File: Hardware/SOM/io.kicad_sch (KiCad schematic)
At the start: 1 part, among them U1 LFE5UM5G-85F-8BG381x

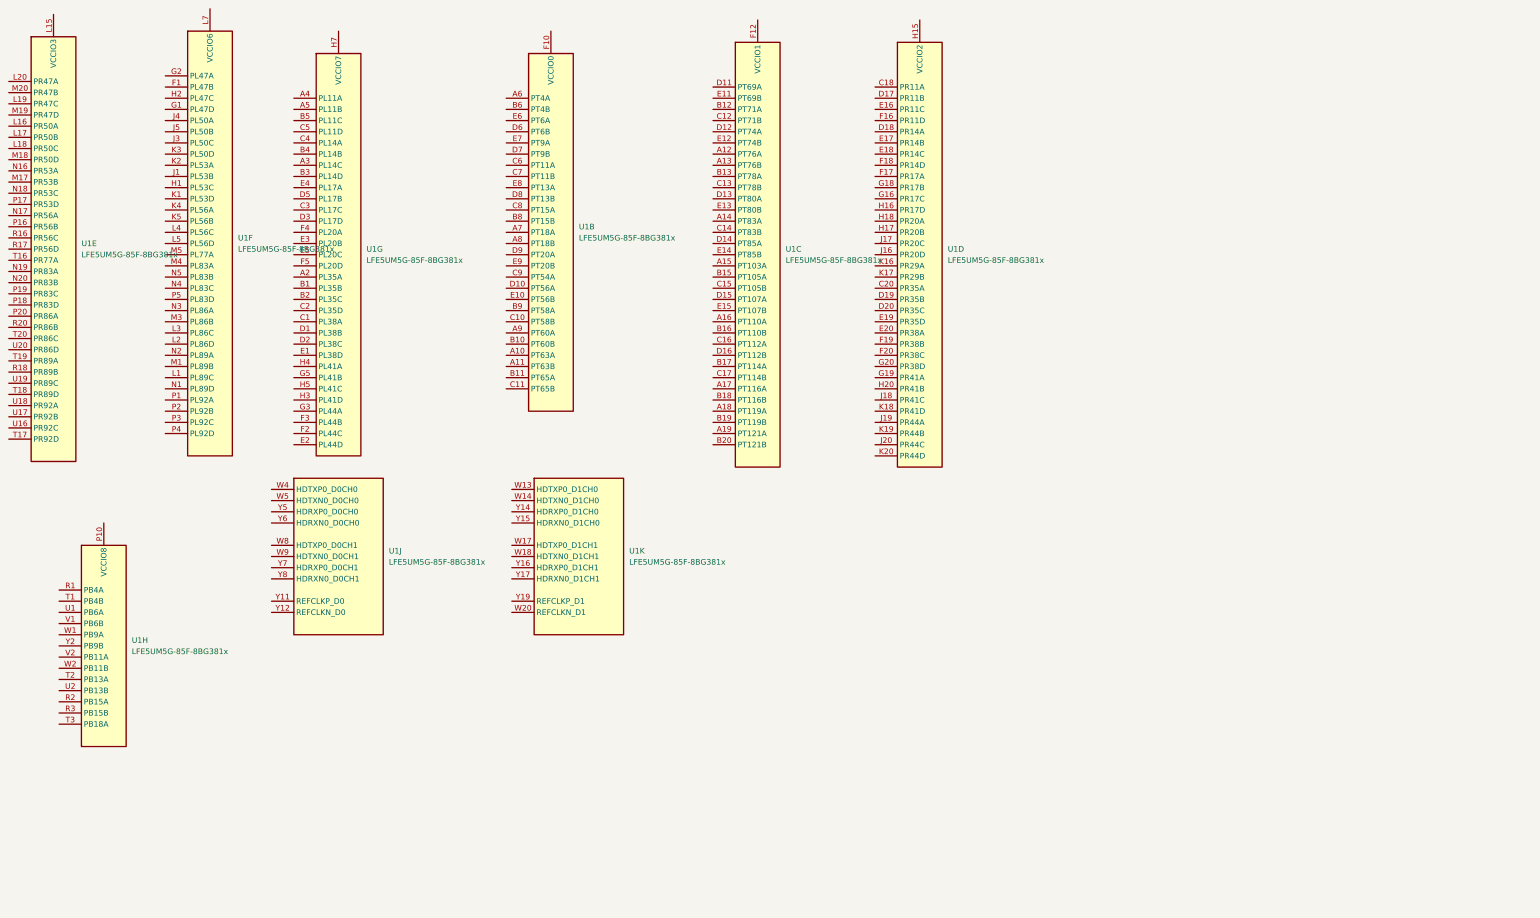
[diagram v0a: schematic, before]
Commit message: SOM: +DDR IC
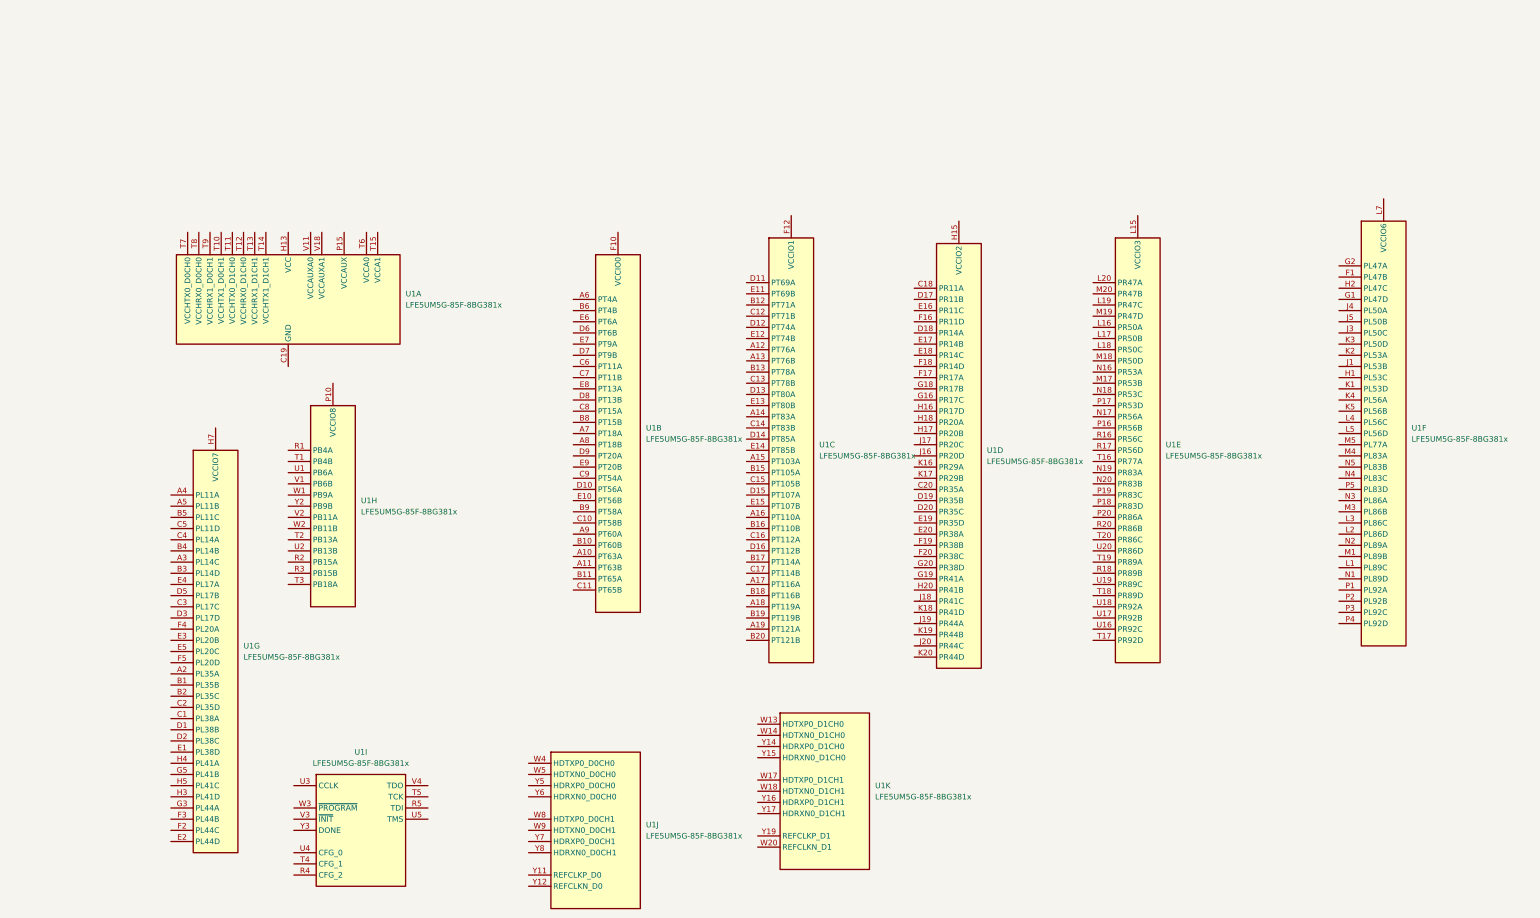
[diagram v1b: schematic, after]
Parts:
- added unit 1 of U1
- added unit 9 of U1
- U1: footprint Package_BGA:Lattice_caBGA-381_17.0x17.0mm_Layout20x20_P0.8mm_Ball0.4mm_Pad0.4mm_NSMD -> Package_BGA:Lattice_caBGA-381_17x17mm_Layout20x20_P0.8mm
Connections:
- new net: U1.B14 (GND), U1.B7 (GND), U1.C19 (GND), U1.D4 (GND), U1.F13 (GND), U1.F14 (GND), U1.F7 (GND), U1.F8 (GND), U1.G10 (GND), U1.G11 (GND), U1.G12 (GND), U1.G13 (GND), U1.G14 (GND), U1.G15 (GND), U1.G17 (GND), U1.G4 (GND), U1.G6 (GND), U1.G7 (GND), U1.G8 (GND), U1.G9 (GND), U1.H19 (GND), U1.J10 (GND), U1.J11 (GND), U1.J12 (GND), U1.J14 (GND), U1.J2 (GND), U1.J7 (GND), U1.J9 (GND), U1.K10 (GND), U1.K11 (GND), U1.K12 (GND), U1.K14 (GND), U1.K15 (GND), U1.K6 (GND), U1.K7 (GND), U1.K9 (GND), U1.L10 (GND), U1.L11 (GND), U1.L12 (GND), U1.L9 (GND), U1.M10 (GND), U1.M11 (GND), U1.M12 (GND), U1.M14 (GND), U1.M16 (GND), U1.M2 (GND), U1.M7 (GND), U1.M9 (GND), U1.N14 (GND), U1.N15 (GND), U1.N6 (GND), U1.N7 (GND), U1.P11 (GND), U1.P12 (GND), U1.P13 (GND), U1.P14 (GND), U1.P7 (GND), U1.P8 (GND), U1.R19 (GND), U1.U10 (GND), U1.U11 (GND), U1.U12 (GND), U1.U13 (GND), U1.U14 (GND), U1.U7 (GND), U1.U8 (GND), U1.U9 (GND), U1.V12 (GND), U1.V13 (GND), U1.V14 (GND), U1.V15 (GND), U1.V16 (GND), U1.V19 (GND), U1.V20 (GND), U1.V5 (GND), U1.V6 (GND), U1.V7 (GND), U1.V8 (GND), U1.V9 (GND), U1.W12 (GND), U1.W15 (GND), U1.W16 (GND), U1.W19 (GND), U1.W6 (GND), U1.W7 (GND)
- new net: U1.F15 (VCCAUX), U1.F6 (VCCAUX), U1.P15 (VCCAUX), U1.P6 (VCCAUX)
- new net: U1.H10 (VCC), U1.H11 (VCC), U1.H12 (VCC), U1.H13 (VCC), U1.H8 (VCC), U1.H9 (VCC), U1.J13 (VCC), U1.J8 (VCC), U1.K13 (VCC), U1.K8 (VCC), U1.L13 (VCC), U1.L8 (VCC), U1.M13 (VCC), U1.M8 (VCC), U1.N10 (VCC), U1.N11 (VCC), U1.N12 (VCC), U1.N13 (VCC), U1.N8 (VCC), U1.N9 (VCC)
- new net: U1.T15 (VCCA1), U1.U15 (VCCA1)
- new net: U1.T6 (VCCA0), U1.U6 (VCCA0)
- new net: U1.V10 (VCCAUXA0), U1.V11 (VCCAUXA0)
- new net: U1.V17 (VCCAUXA1), U1.V18 (VCCAUXA1)
